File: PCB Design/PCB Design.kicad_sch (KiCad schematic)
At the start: 37 parts, among them J1 Conn_01x02_Pin, J2 DX07S024WJ3R400, J4 Conn_02x16_Odd_Even, Q1 2N7002, Q2 2N7002, U1 INA219AxD, U2 IP2721, U3 DRV8833PW, U4 AP22818AKEWT, U5 AP22818AKEWT, U6 DRV8833PW, U7 BQ21040DBV

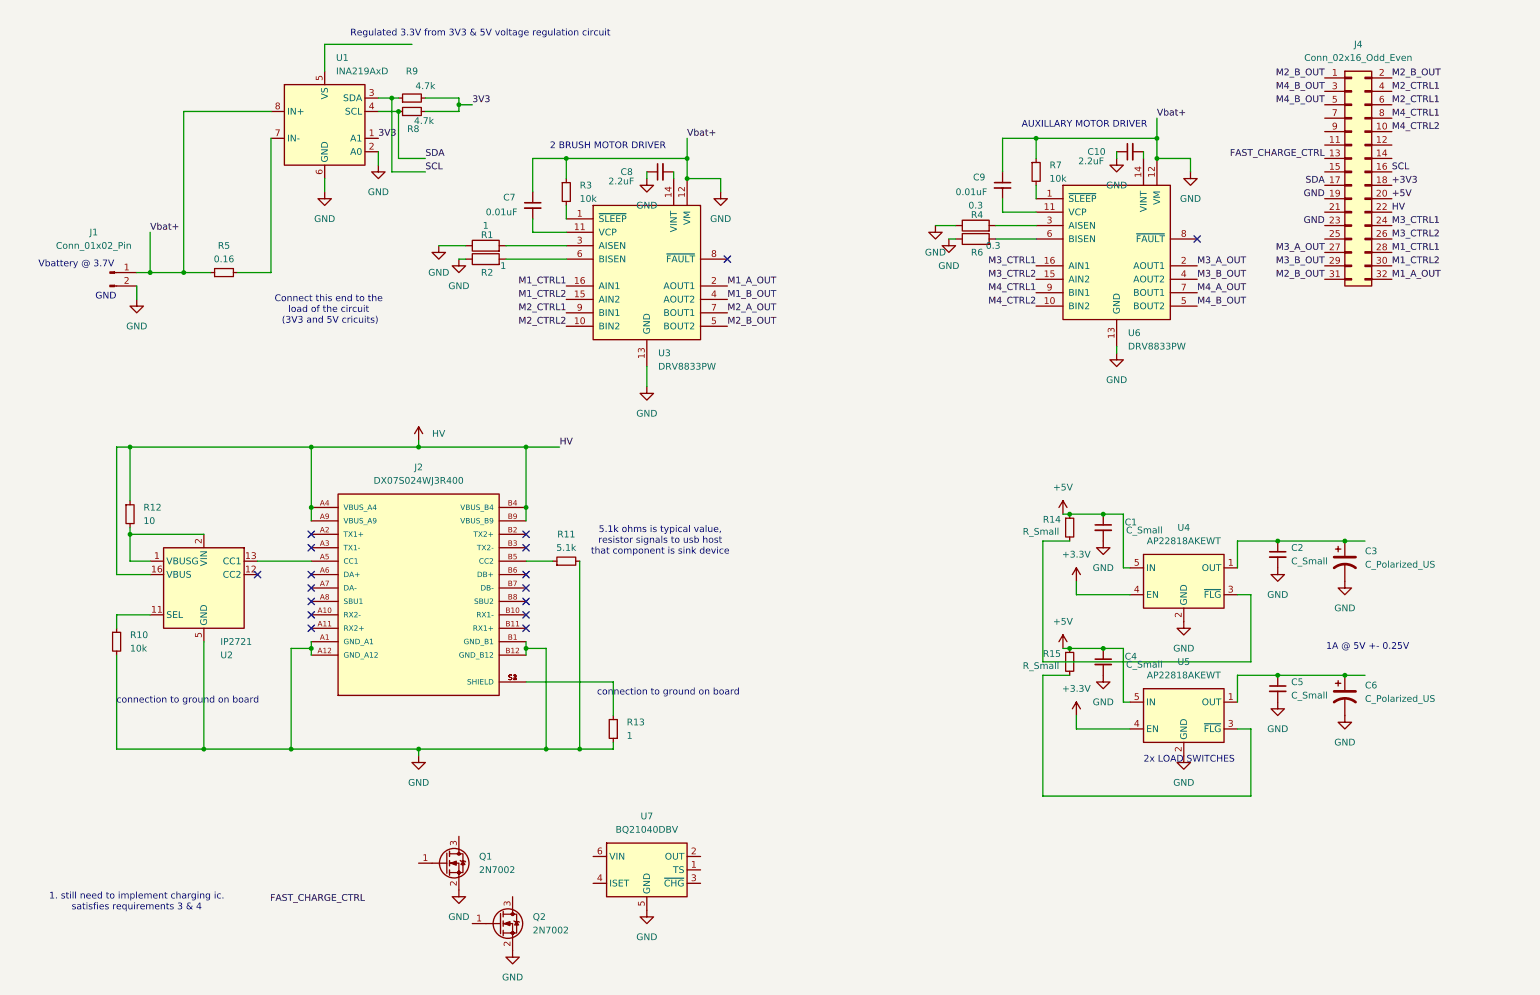
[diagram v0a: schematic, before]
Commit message: Added 9V to 5V and 5V to 3V3 regulators. Added charging IC and fast charging circuitry to overall charging circuit.
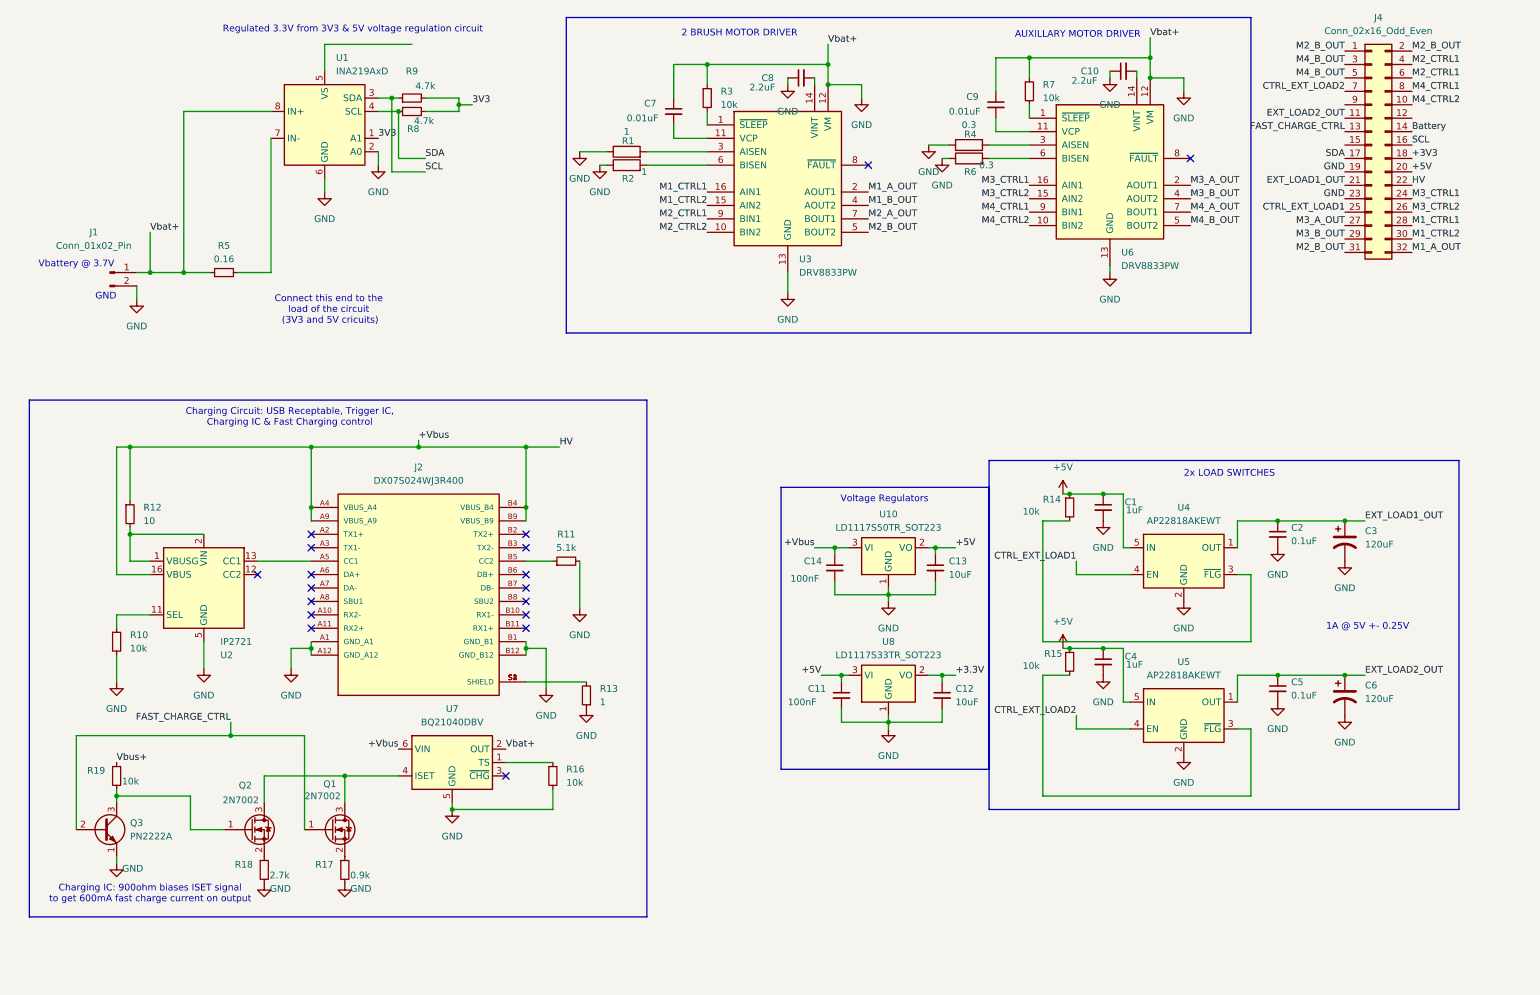
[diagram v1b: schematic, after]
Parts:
- added C11, C14: 100nF, symbol Device:C_Small
- added C12, C13: 10uF, symbol Device:C_Small
- added Q3: PN2222A, Package_TO_SOT_THT:TO-92_Inline, symbol Transistor_BJT:PN2222A
- added R16, R19: 10k, symbol Device:R_Small
- added R17: 0.9k, symbol Device:R_Small
- added R18: 2.7k, symbol Device:R_Small
- added U10: LD1117S50TR_SOT223, Package_TO_SOT_SMD:SOT-223-3_TabPin2, symbol Regulator_Linear:LD1117S50TR_SOT223
- added U8: LD1117S33TR_SOT223, Package_TO_SOT_SMD:SOT-223-3_TabPin2, symbol Regulator_Linear:LD1117S33TR_SOT223
- C1, C4: value C_Small -> 1uF
- C2, C5: value C_Small -> 0.1uF
- C3, C6: value C_Polarized_US -> 120uF
- R14, R15: value R_Small -> 10k
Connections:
- net HV is gone; now on net +Vbus: J2.A4 (VBUS_A4), J2.A9 (VBUS_A9), J2.B4 (VBUS_B4), J2.B9 (VBUS_B9), J4.22 (Pin_22), R12.1, U2.16 (VBUS)
- net +3.3V: now also C12.1, U8.2 (VO); no longer U4.4 (EN), U5.4 (EN)
- net +5V: now also C11.1, C13.1, U10.2 (VO), U8.3 (VI)
- net FAST_CHARGE_CTRL: now also Q1.1 (G), Q3.2 (B)
- net GND: now also U7.2 (OUT), C11.2, C12.2, C13.2, C14.2, Q3.1 (E), R16.2, R17.2, R18.2, U10.1 (GND), U8.1 (GND); no longer Q1.2 (S), Q2.2 (S)
- net EXT_LOAD2_OUT: now reaches C5.1, C6.1, U5.1 (OUT)
- net EXT_LOAD2_OUT: now also J4.11 (Pin_11)
- net EXT_LOAD1_OUT: now reaches C2.1, C3.1, U4.1 (OUT)
- net EXT_LOAD1_OUT: now also J4.21 (Pin_21)
- net at Q2.1 (G): now also Q3.3 (C), R19.2
- net at Q2.3 (D): now also Q1.3 (D), U7.4 (ISET)
- net Battery: now reaches J4.14 (Pin_14)
- net CTRL_EXT_LOAD1: now reaches J4.25 (Pin_25)
- net CTRL_EXT_LOAD1: now also U4.4 (EN)
- net CTRL_EXT_LOAD2: now reaches J4.7 (Pin_7)
- net CTRL_EXT_LOAD2: now also U5.4 (EN)
- net at U7.1 (TS): now also R16.1
- net +Vbus: now reaches U7.6 (VIN)
- net +Vbus: now also C14.1, U10.3 (VI)
- new net: Q1.2 (S), R17.1
- new net: Q2.2 (S), R18.1
- new net Vbus+: R19.1
- no-connect marks 17 -> 18
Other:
- note added: "Charging Circuit: USB Receptable, Trigger IC, Charging IC & Fast Charging control"
- note added: "Charging IC: 900ohm biases ISET signal to get 600mA fast charge current on output"
- note added: "Voltage Regulators"
- note removed: "1. still need to implement charging ic. satisfies requirements 3 & 4"
- note removed: "5.1k ohms is typical value, resistor signals to usb host that component is sink device"
- note removed: "connection to ground on board"
- moved on the sheet: C1, C10, C2, C3, C7, C8, C9, J4, Q1, Q2, R1, R13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

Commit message: Fixed capacitor of INA219 configuration
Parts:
- removed J1: Conn_01x02_Pin, symbol Connector:Conn_01x02_Pin
- added C15: 0.1uF, symbol Device:C_Small
- R8, R9: value 4.7k -> 3.3k
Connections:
- net Battery is gone; now on net GND: J4.14 (Pin_14)
- net +3.3V: now also R8.2, R9.2, U1.5 (VS), C15.1
- net +Vbus: no longer C14.1, U10.3 (VI)
- net 3V3: no longer R8.2, R9.2
- net GND: now also C15.2
- net load: now reaches R5.2, U1.7 (IN-)
- net load: now also C14.1, U10.3 (VI)
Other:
- note removed: "GND"
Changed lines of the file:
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@@
 		)
 	)
-	(text "GND"
-		(exclude_from_sim no)
-		(at 27.178 66.802 0)
-		(effects
-			(font
-				(size 1.27 1.27)
-			)
-		)
-	)
 	(text "1A @ 5V +- 0.25V"
 		(exclude_from_sim no)
@@
 	(text "Vbattery @ 3.7V"
 		(exclude_from_sim no)
-		(at 21.59 60.706 0)
+		(at 24.13 44.45 0)
 		(effects
 			(font
@@
 	)
 	(junction
-		(at 35.56 62.23)
-		(diameter 0)
-		(color 0 0 0 0)
-	)
-	(junction
 		(at 106.68 106.68)
 		(diameter 0)
@@
 	)
 	(junction
+		(at 97.79 30.48)
+		(diameter 0)
+		(color 0 0 0 0)
+	)
+	(junction
 		(at 215.9 104.14)
 		(diameter 0)
@@
 	(wire
 		(pts
+			(xy 97.79 30.48) (xy 93.98 30.48)
+		)
+		(stroke
+			(width 0)
+			(type default)
+		)
+	)
+	(wire
+		(pts
 			(xy 78.74 41.91) (xy 78.74 39.37)
 		)
@@
 	(wire
 		(pts
-			(xy 33.02 64.77) (xy 33.02 67.31)
-		)
-		(stroke
-			(width 0)
-			(type default)
-		)
-	)
-	(wire
-		(pts
 			(xy 201.93 21.59) (xy 201.93 25.4)
 		)
@@
 	(wire
 		(pts
-			(xy 33.02 62.23) (xy 35.56 62.23)
-		)
-		(stroke
-			(width 0)
-			(type default)
-		)
-	)
-	(wire
-		(pts
 			(xy 58.42 31.75) (xy 41.91 31.75)
 		)
@@
 	(wire
 		(pts
-			(xy 96.52 30.48) (xy 93.98 30.48)
+			(xy 104.14 30.48) (xy 97.79 30.48)
 		)
 		(stroke
@@
 		)
 	)
-	(label "3V3"
-		(at 96.52 30.48 0)
+	(label "M2_B_OUT"
+		(at 261.62 20.32 180)
 		(effects
 			(font
 				(size 1.27 1.27)
-				(color 0 58 255 1)
 			)
-			(justify left bottom)
+			(justify right bottom)
 		)
 	)
-	(label "M2_B_OUT"
-		(at 261.62 20.32 180)
+	(label "load"
+		(at 58.42 62.23 0)
 		(effects
 			(font
 				(size 1.27 1.27)
 			)
-			(justify right bottom)
+			(justify left bottom)
 		)
 	)
@@
 		)
 	)
-	(label "+Vbus"
+	(label "load"
 		(at 161.29 114.3 180)
 		(effects
@@
 		)
 	)
+	(label "+3.3V"
+		(at 104.14 30.48 0)
+		(effects
+			(font
+				(size 1.27 1.27)
+			)
+			(justify left bottom)
+		)
+	)
 	(label "M2_CTRL1"
 		(at 140.97 52.07 180)
@@
 		)
 	)
-	(label "Battery"
+	(label "Vbat+"
 		(at 274.32 35.56 0)
 		(effects
@@
 		)
 	)
+	(label "+3.3V"
+		(at 85.09 19.05 0)
+		(effects
+			(font
+				(size 1.27 1.27)
+			)
+			(justify left bottom)
+		)
+	)
 	(label "+Vbus"
 		(at 86.36 93.98 0)
@@
 			)
 		)
-		(property "Value" "4.7k"
+		(property "Value" "3.3k"
 			(at 87.376 33.528 90)
 			(effects
@@
 	)
 	(symbol
+		(lib_id "power:GND")
+		(at 97.79 35.56 0)
+		(unit 1)
+		(exclude_from_sim no)
+		(in_bom yes)
+		(on_board yes)
+		(dnp no)
+		(fields_autoplaced yes)
+		(property "Reference" "#PWR05"
+			(at 97.79 41.91 0)
+			(effects
+				(font
+					(size 1.27 1.27)
+				)
+				(hide yes)
+			)
+		)
+		(property "Value" "GND"
+			(at 97.79 40.64 0)
+			(effects
+				(font
+					(size 1.27 1.27)
+				)
+			)
+		)
+		(property "Footprint" ""
+			(at 97.79 35.56 0)
+			(effects
+				(font
+					(size 1.27 1.27)
+				)
+				(hide yes)
+			)
+		)
+		(property "Datasheet" ""
+			(at 97.79 35.56 0)
+			(effects
+				(font
+					(size 1.27 1.27)
+				)
+				(hide yes)
+			)
+		)
+		(property "Description" "Power symbol creates a global label with name \"GND\" , ground"
+			(at 97.79 35.56 0)
+			(effects
+				(font
+					(size 1.27 1.27)
+				)
+				(hide yes)
+			)
+		)
+		(pin "1"
+		)
+		(instances
+			(project ""
+				(path "/09a634de-0d1e-4622-9f3f-daf978711512"
+					(reference "#PWR05")
+					(unit 1)
+				)
+			)
+		)
+	)
+	(symbol
 		(lib_id "Device:R_Small")
 		(at 72.39 175.26 0)
@@
 	)
 	(symbol
-		(lib_id "Connector:Conn_01x02_Pin")
-		(at 27.94 62.23 0)
-		(unit 1)
-		(exclude_from_sim no)
-		(in_bom yes)
-		(on_board yes)
-		(dnp no)
-		(property "Reference" "J1"
-			(at 24.892 54.61 0)
-			(effects
-				(font
-					(size 1.27 1.27)
-				)
-			)
-		)
-		(property "Value" "Conn_01x02_Pin"
-			(at 24.892 57.15 0)
-			(effects
-				(font
-					(size 1.27 1.27)
-				)
-			)
-		)
-		(property "Footprint" ""
-			(at 27.94 62.23 0)
-			(effects
-				(font
-					(size 1.27 1.27)
-				)
-				(hide yes)
-			)
-		)
-		(property "Datasheet" "~"
-			(at 27.94 62.23 0)
-			(effects
-				(font
-					(size 1.27 1.27)
-				)
-				(hide yes)
-			)
-		)
-		(property "Description" "Generic connector, single row, 01x02, script generated"
-			(at 27.94 62.23 0)
-			(effects
-				(font
-					(size 1.27 1.27)
-				)
-				(hide yes)
-			)
-		)
-		(pin "2"
-		)
-		(pin "1"
-		)
-		(instances
-			(project ""
-				(path "/09a634de-0d1e-4622-9f3f-daf978711512"
-					(reference "J1")
-					(unit 1)
-				)
-			)
-		)
-	)
-	(symbol
 		(lib_id "Device:R_Small")
 		(at 49.53 62.23 90)
@@
 			)
 		)
-		(property "Value" "4.7k"
+		(property "Value" "3.3k"
 			(at 87.63 26.924 90)
 			(effects
@@
 	)
 	(symbol
-		(lib_id "power:GND")
-		(at 33.02 67.31 0)
-		(unit 1)
-		(exclude_from_sim no)
-		(in_bom yes)
-		(on_board yes)
-		(dnp no)
-		(fields_autoplaced yes)
-		(property "Reference" "#PWR05"
-			(at 33.02 73.66 0)
-			(effects
-				(font
-					(size 1.27 1.27)
-				)
-				(hide yes)
-			)
-		)
-		(property "Value" "GND"
-			(at 33.02 72.39 0)
-			(effects
-				(font
-					(size 1.27 1.27)
-				)
-			)
-		)
-		(property "Footprint" ""
-			(at 33.02 67.31 0)
-			(effects
-				(font
-					(size 1.27 1.27)
-				)
-				(hide yes)
-			)
-		)
-		(property "Datasheet" ""
-			(at 33.02 67.31 0)
-			(effects
-				(font
-					(size 1.27 1.27)
-				)
-				(hide yes)
-			)
-		)
-		(property "Description" "Power symbol creates a global label with name \"GND\" , ground"
-			(at 33.02 67.31 0)
-			(effects
-				(font
-					(size 1.27 1.27)
-				)
-				(hide yes)
-			)
-		)
-		(pin "1"
-		)
-		(instances
-			(project ""
-				(path "/09a634de-0d1e-4622-9f3f-daf978711512"
-					(reference "#PWR05")
-					(unit 1)
-				)
-			)
-		)
-	)
-	(symbol
 		(lib_id "Device:C_Small")
 		(at 248.92 111.76 0)
@@
 					(unit 1)
 				)
+			)
+		)
+	)
+	(symbol
+		(lib_id "Device:C_Small")
+		(at 97.79 33.02 0)
+		(unit 1)
+		(exclude_from_sim no)
+		(in_bom yes)
+		(on_board yes)
+		(dnp no)
+		(fields_autoplaced yes)
+		(property "Reference" "C15"
+			(at 100.33 31.7562 0)
+			(effects
+				(font
+					(size 1.27 1.27)
+				)
+				(justify left)
+			)
+		)
+		(property "Value" "0.1uF"
+			(at 100.33 34.2962 0)
+			(effects
+				(font
+					(size 1.27 1.27)
+				)
+				(justify left)
+			)
+		)
+		(property "Footprint" ""
+			(at 97.79 33.02 0)
+			(effects
+				(font
+					(size 1.27 1.27)
+				)
+				(hide yes)
+			)
+		)
+		(property "Datasheet" "~"
+			(at 97.79 33.02 0)
+			(effects
+				(font
+					(size 1.27 1.27)
+				)
+				(hide yes)
+			)
+		)
+		(property "Description" "Unpolarized capacitor, small symbol"
+			(at 97.79 33.02 0)
+			(effects
+				(font
+					(size 1.27 1.27)
+				)
+				(hide yes)
+			)
+		)
+		(pin "2"
+		)
+		(pin "1"
+		)
+		(instances
+			(project ""
+				(path "/09a634de-0d1e-4622-9f3f-daf978711512"
+					(reference "C15")
+					(unit 1)
+				)
